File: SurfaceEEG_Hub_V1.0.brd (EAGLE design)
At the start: 30 x 26 mm, 15 parts, among them IC1 LMP7702, P2 SOLDERPAD4-1.27-2.54, P3 SOLDERPAD4-1.27-2.54, P4 SOLDERPAD4-1.27-2.54

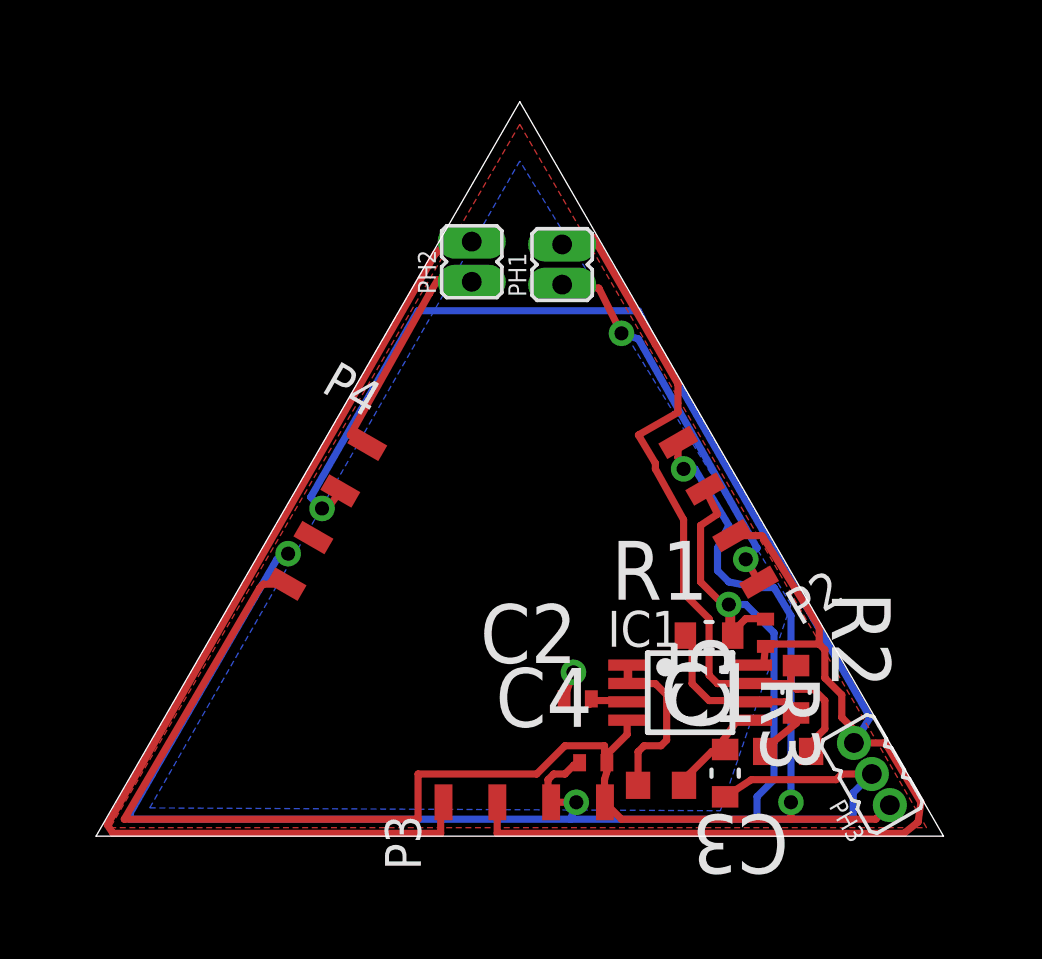
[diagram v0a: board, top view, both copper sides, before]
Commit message: Fixed hub module according to DRC
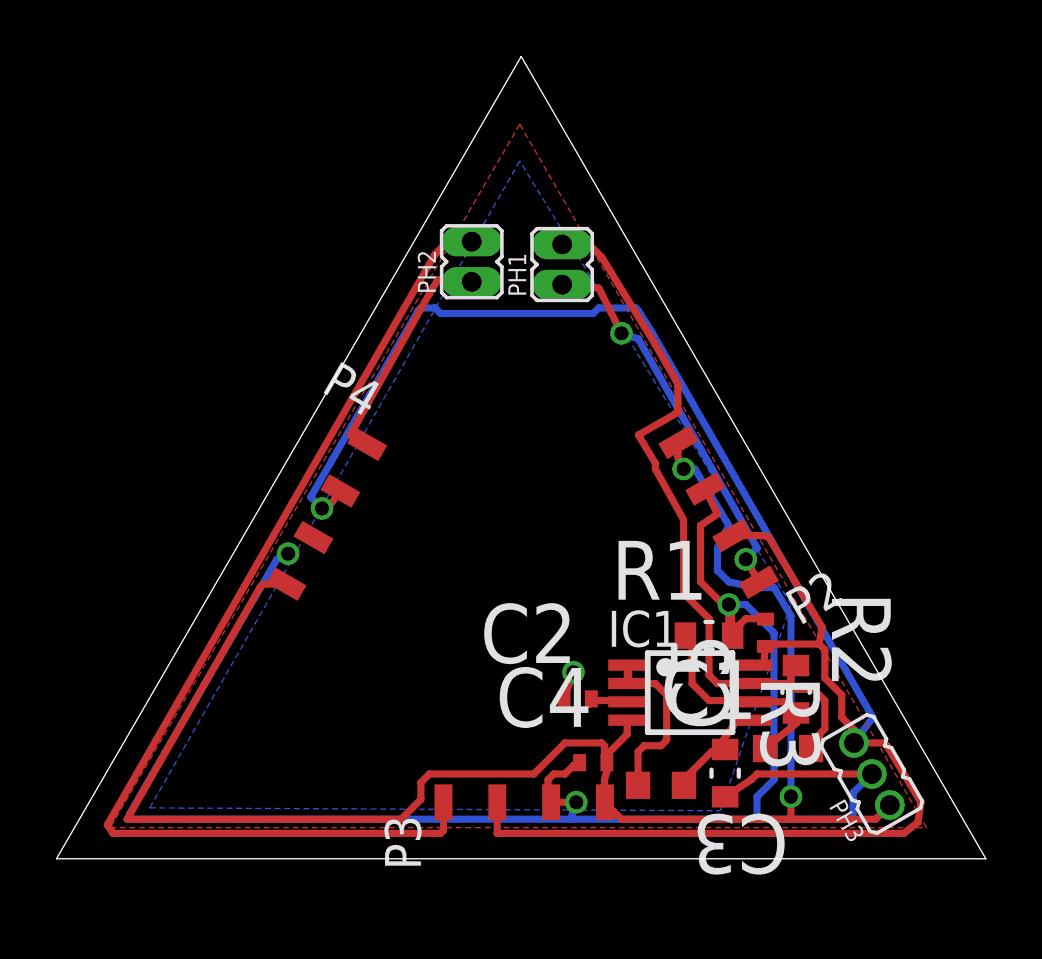
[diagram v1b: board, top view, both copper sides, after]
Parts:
- moved C1 0.10 mm to (42.7, 20.3)
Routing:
- net GND: track 59.9 -> 59.2 mm
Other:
- board size 30 x 26 mm -> 32.9 x 28.4 mm
